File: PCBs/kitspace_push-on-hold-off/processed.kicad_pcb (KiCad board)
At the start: 2 copper layers, 22.9 x 12.7 mm, 17 parts, among them P1 CONN_01X04, P2 CONN_01X04, Q1 IRF7309IPBF, SW1 SW_PUSH_SMALL

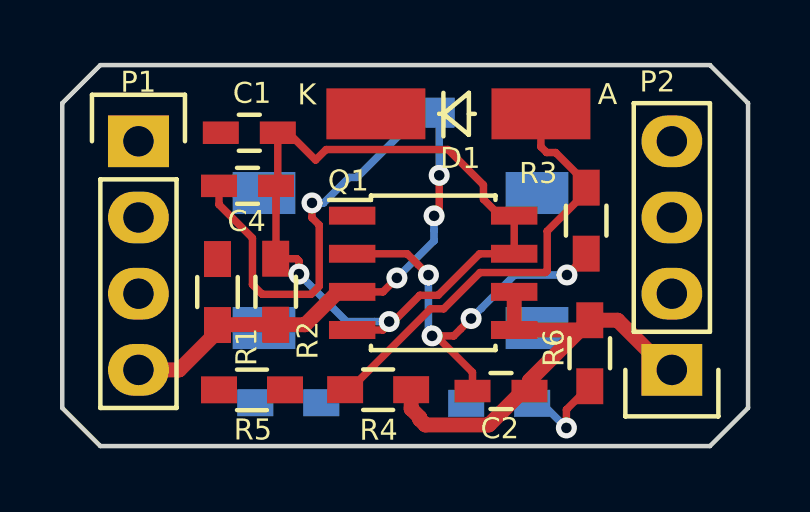
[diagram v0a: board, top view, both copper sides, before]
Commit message: recheck all circuits and clean up fill zone by rerouting the nets using freerouting and manually
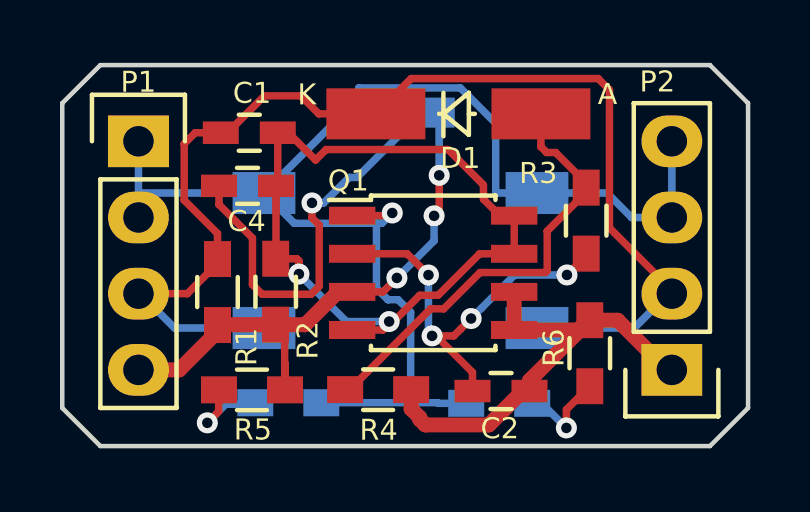
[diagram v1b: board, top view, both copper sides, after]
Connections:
- C1 pad 2: (no net) -> /Button
- D1 pad 1: (no net) -> /Button
- JP1 pad 1: (no net) -> GND
- LED1 pad 1: (no net) -> GND
- LED1 pad 2: (no net) -> Net-(LED1-Pad2)
- LED2 pad 1: (no net) -> GND
- P1 pad 1: (no net) -> GND
- P1 pad 2: (no net) -> GND
- P1 pad 3: (no net) -> /Button
- P2 pad 2: (no net) -> /Button
- P2 pad 3: (no net) -> GND
- P2 pad 4: (no net) -> GND
- Q1 pad 1: (no net) -> GND
- R1 pad 2: (no net) -> /Button
- R5 pad 1: (no net) -> /Vin
- R5 pad 2: (no net) -> Net-(LED1-Pad2)
- SW1 pad 1: (no net) -> /Button
- SW1 pad 2: (no net) -> GND
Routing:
- net GND: track 0.00 -> 45.8 mm, vias 0 -> 1
- net /Button: track 0.00 -> 41.5 mm
- net Net-(LED1-Pad2): track 0.00 -> 3.47 mm, vias 0 -> 1
- net /Vin: track 33.7 -> 36.8 mm
- net /Vout: track 16.5 -> 17.1 mm
- net Net-(LED2-Pad2): track 3.19 -> 3.79 mm
- net Net-(D1-Pad2): track 14.9 -> 15.5 mm
